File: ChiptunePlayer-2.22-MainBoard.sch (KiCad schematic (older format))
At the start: 7 parts, among them J1 USB_OTG

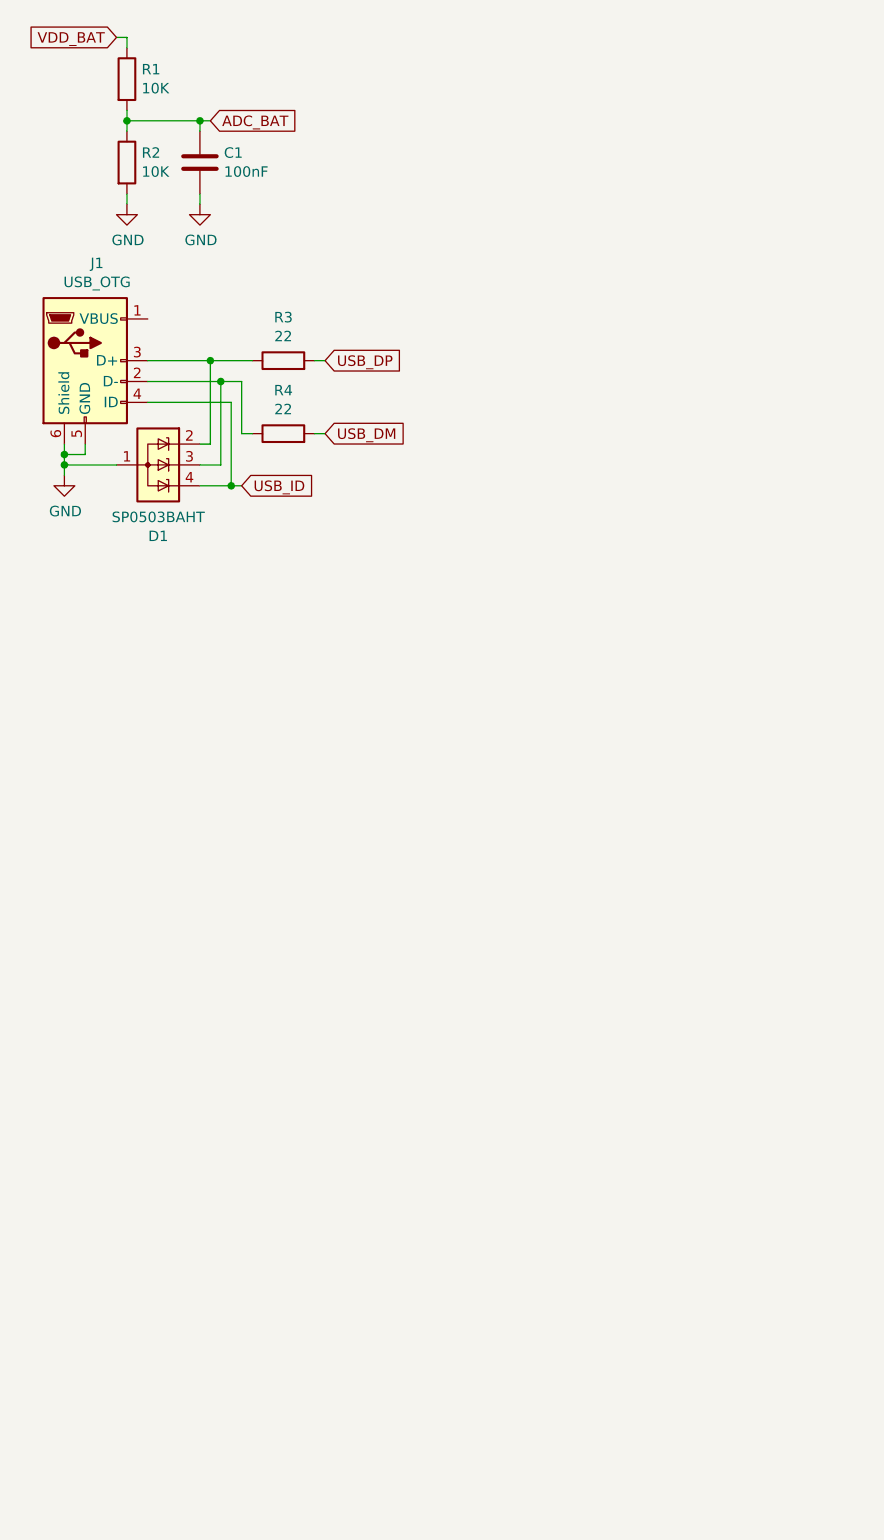
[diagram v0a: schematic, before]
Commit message: Добавлена часть зарядки, клавиши +-, поправлен USB, все разделено на вложенные листи.
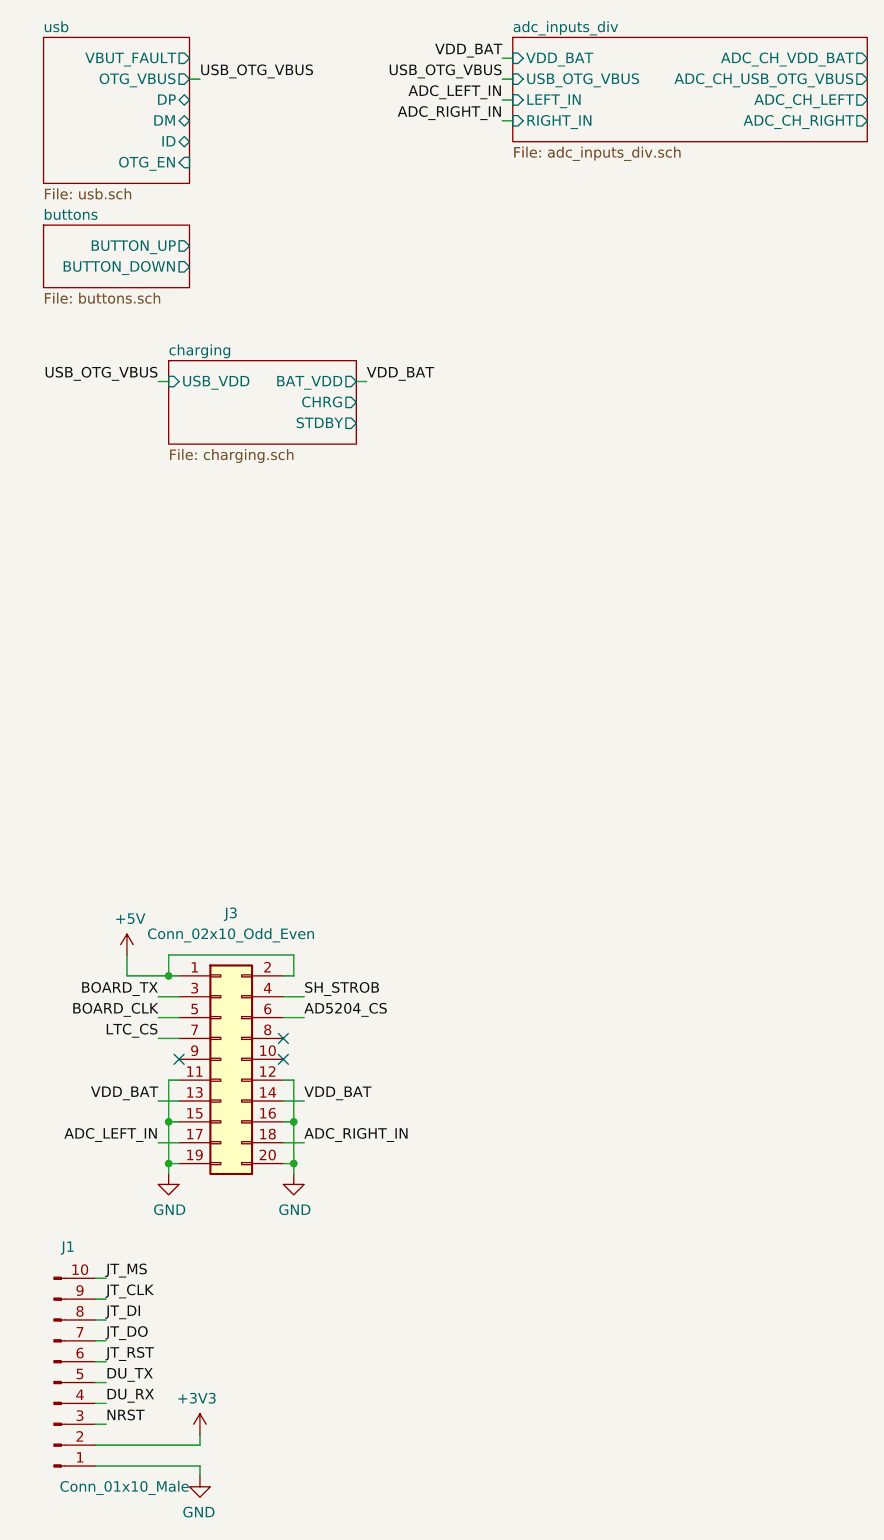
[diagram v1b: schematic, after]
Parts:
- removed C1: 100nF, Capacitor_SMD:C_0603_1608Metric_Pad1.05x0.95mm_HandSolder, symbol Device:C
- removed D1: SP0503BAHT, Package_TO_SOT_SMD:SOT-143, symbol Power_Protection:SP0503BAHT
- removed J1: USB_OTG, Connector_USB:USB_Mini-B_Wuerth_65100516121_Horizontal, symbol Connector:USB_OTG
- removed R1, R2: 10K, Resistor_SMD:R_0603_1608Metric_Pad1.05x0.95mm_HandSolder, symbol Device:R
- removed R3, R4: 22, Resistor_SMD:R_0603_1608Metric_Pad1.05x0.95mm_HandSolder, symbol Device:R
- added J1: Conn_01x10_Male, Connector_PinHeader_2.54mm:PinHeader_1x10_P2.54mm_Horizontal, symbol Connector:Conn_01x10_Male
- added J3: Conn_02x10_Odd_Even, Connector_PinHeader_2.54mm:PinHeader_2x10_P2.54mm_Vertical_SMD, symbol Connector_Generic:Conn_02x10_Odd_Even
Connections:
- net GND: now also J1.1 (Pin_1), J3.11 (Pin_11), J3.12 (Pin_12), J3.15 (Pin_15), J3.16 (Pin_16), J3.19 (Pin_19), J3.20 (Pin_20)
- net VDD_BAT: now also J3.13 (Pin_13), J3.14 (Pin_14)
- new net +3V3: J1.2 (Pin_2)
- new net +5V: J3.1 (Pin_1), J3.2 (Pin_2)
- new net AD5204_CS: J3.6 (Pin_6)
- new net ADC_LEFT_IN: J3.17 (Pin_17)
- new net ADC_RIGHT_IN: J3.18 (Pin_18)
- new net BOARD_CLK: J3.5 (Pin_5)
- new net BOARD_TX: J3.3 (Pin_3)
- new net DU_RX: J1.4 (Pin_4)
- new net DU_TX: J1.5 (Pin_5)
- new net JT_CLK: J1.9 (Pin_9)
- new net JT_DI: J1.8 (Pin_8)
- new net JT_DO: J1.7 (Pin_7)
- new net JT_MS: J1.10 (Pin_10)
- new net JT_RST: J1.6 (Pin_6)
- new net LTC_CS: J3.7 (Pin_7)
- new net NRST: J1.3 (Pin_3)
- new net SH_STROB: J3.4 (Pin_4)
- no-connect marks 0 -> 3

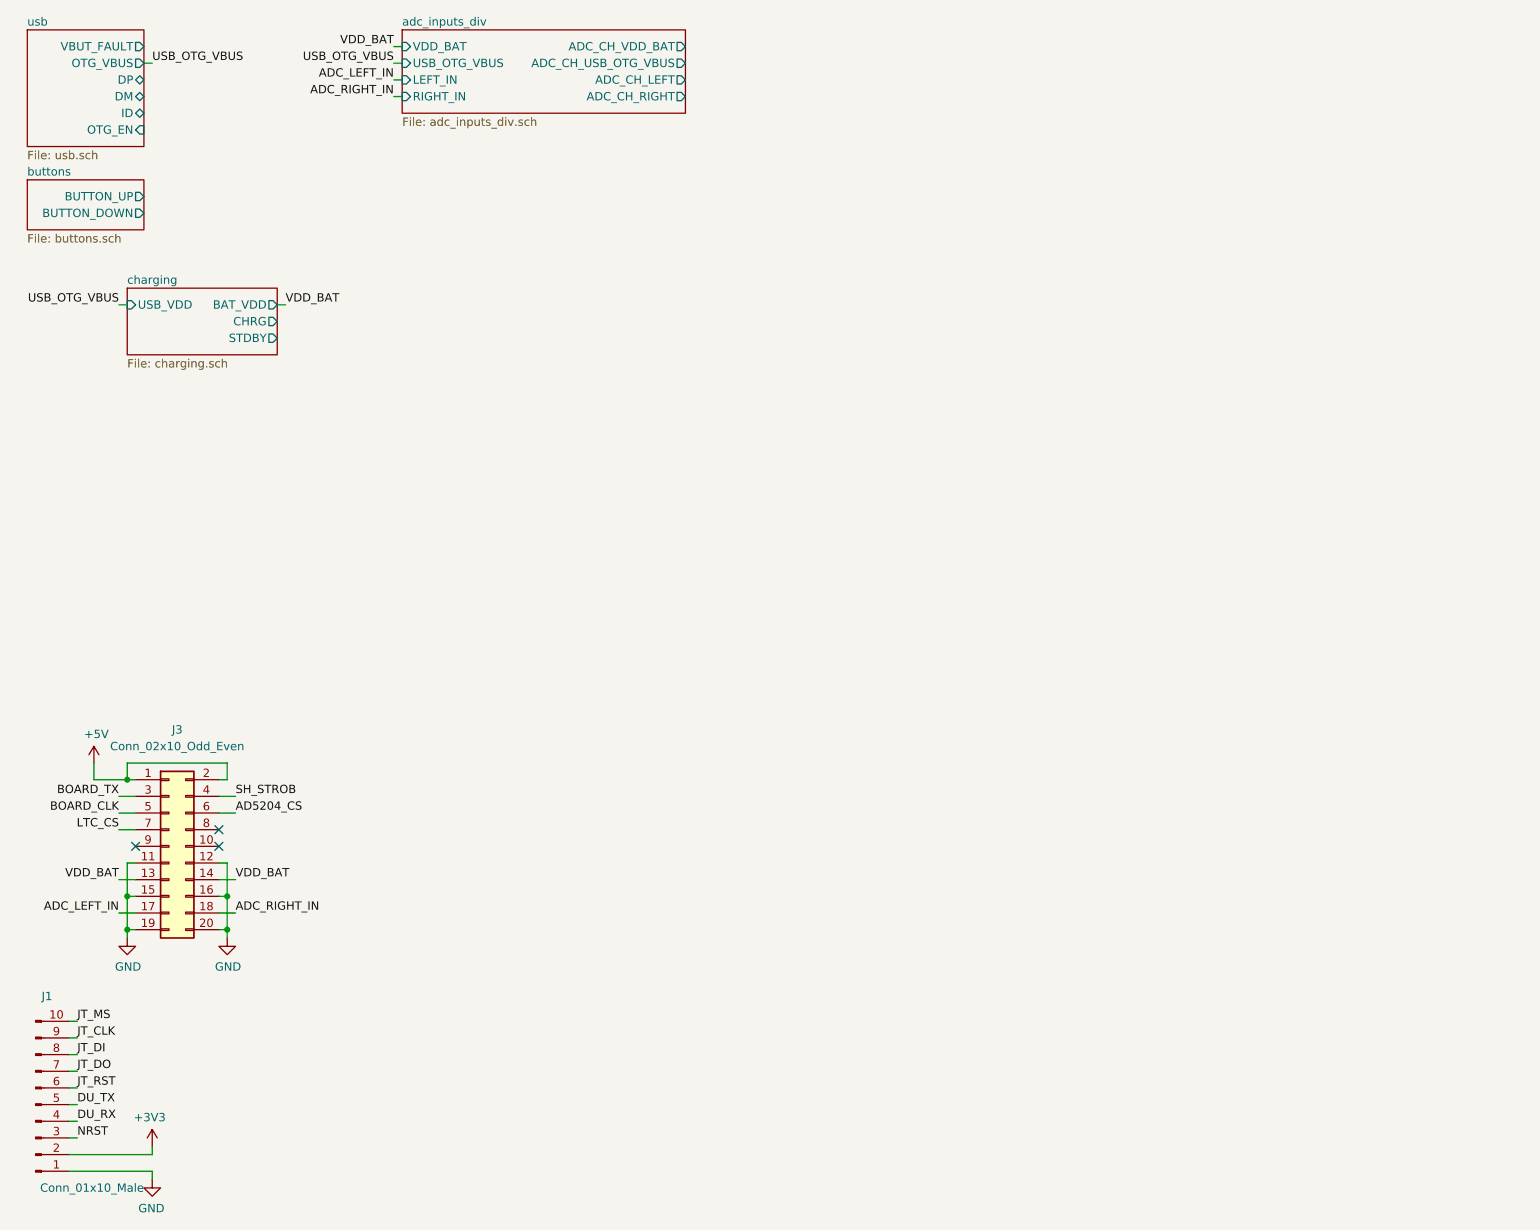
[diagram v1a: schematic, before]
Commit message: Запитал МК, добавил цепи питания, тактирования, модуль клавиатуры.
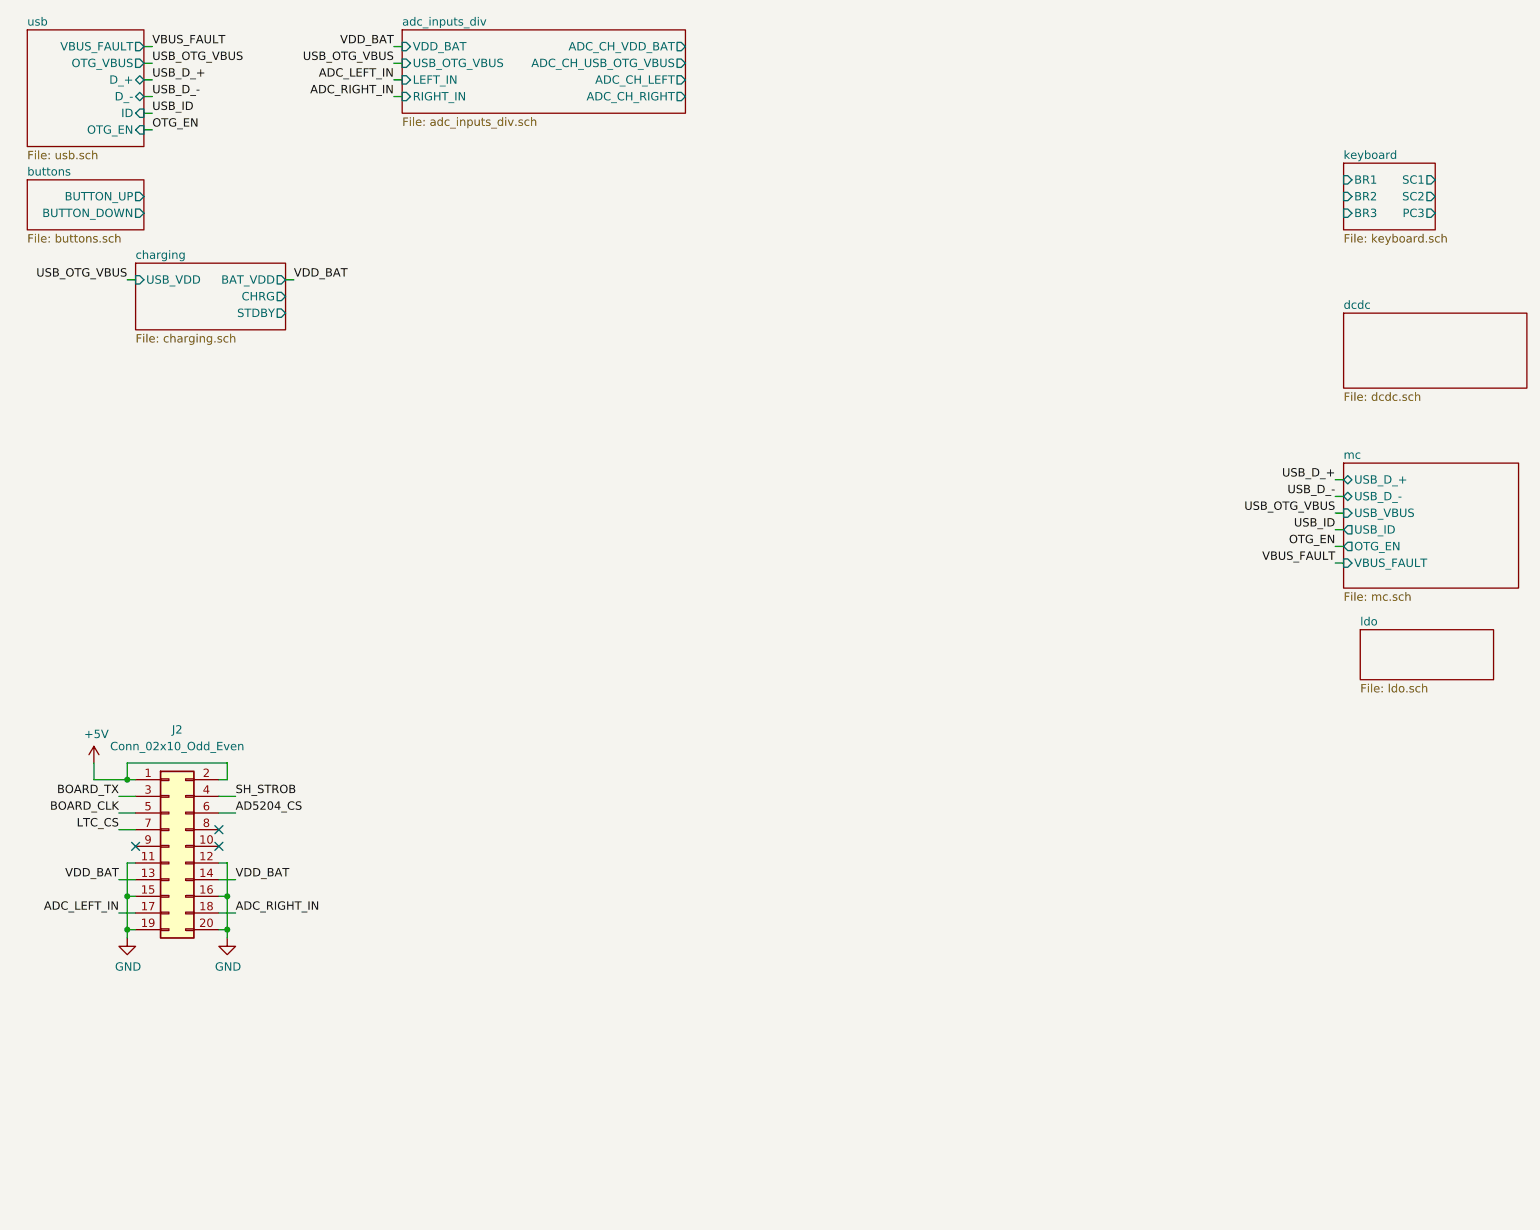
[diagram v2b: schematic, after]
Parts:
- removed J1: Conn_01x10_Male, Connector_PinHeader_2.54mm:PinHeader_1x10_P2.54mm_Horizontal, symbol Connector:Conn_01x10_Male
- renumbered J3 to J2
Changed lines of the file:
@@
 $Descr A4 11693 8268
 encoding utf-8
-Sheet 1 5
+Sheet 1 9
 Title ""
 Date "2020-04-18"
@@
 $EndDescr
 $Comp
-L Connector:Conn_01x10_Male J1
-U 1 1 5EA8D1A2
-P 600 7050
-F 0 "J1" H 700 6400 50  0000 R CNN
-F 1 "Conn_01x10_Male" H 1250 7550 50  0000 R CNN
-F 2 "Connector_PinHeader_2.54mm:PinHeader_1x10_P2.54mm_Horizontal" H 600 7050 50  0001 C CNN
-F 3 "~" H 600 7050 50  0001 C CNN
-	1    600  7050
-	1    0    0    1
-$EndComp
-$Comp
-L power:GND #PWR02
-U 1 1 5EA97B30
-P 1300 7500
-F 0 "#PWR02" H 1300 7250 50  0001 C CNN
-F 1 "GND" H 1305 7327 50  0000 C CNN
-F 2 "" H 1300 7500 50  0001 C CNN
-F 3 "" H 1300 7500 50  0001 C CNN
-	1    1300 7500
-	-1   0    0    -1
-$EndComp
-$Comp
-L power:+3V3 #PWR01
-U 1 1 5EA9CF13
-P 1300 7300
-F 0 "#PWR01" H 1300 7150 50  0001 C CNN
-F 1 "+3V3" H 1315 7473 50  0000 C CNN
-F 2 "" H 1300 7300 50  0001 C CNN
-F 3 "" H 1300 7300 50  0001 C CNN
-	1    1300 7300
-	-1   0    0    -1
-$EndComp
-Wire Wire Line
-	800  7450 1300 7450
-Wire Wire Line
-	1300 7450 1300 7500
-Wire Wire Line
-	1300 7350 1300 7300
-Wire Wire Line
-	1300 7350 800  7350
-Wire Wire Line
-	850  6550 800  6550
-Wire Wire Line
-	850  6650 800  6650
-Wire Wire Line
-	850  6750 800  6750
-Wire Wire Line
-	850  6850 800  6850
-Wire Wire Line
-	850  6950 800  6950
-Wire Wire Line
-	800  7050 850  7050
-Wire Wire Line
-	850  7150 800  7150
-Wire Wire Line
-	850  7250 800  7250
-$Comp
-L power:+5V #PWR03
+L power:+5V #PWR01
 U 1 1 5EABF65B
 P 950 5000
-F 0 "#PWR03" H 950 4850 50  0001 C CNN
+F 0 "#PWR01" H 950 4850 50  0001 C CNN
 F 1 "+5V" H 965 5173 50  0000 C CNN
 F 2 "" H 950 5000 50  0001 C CNN
@@
 $EndComp
 $Comp
-L power:GND #PWR04
+L power:GND #PWR02
 U 1 1 5EAC2A23
 P 1150 6050
-F 0 "#PWR04" H 1150 5800 50  0001 C CNN
+F 0 "#PWR02" H 1150 5800 50  0001 C CNN
 F 1 "GND" H 1155 5877 50  0000 C CNN
 F 2 "" H 1150 6050 50  0001 C CNN
@@
 $EndSheet
 $Comp
-L Connector_Generic:Conn_02x10_Odd_Even J3
+L Connector_Generic:Conn_02x10_Odd_Even J2
 U 1 1 5EA4935C
 P 1400 5500
-F 0 "J3" H 1450 6200 50  0000 C CNN
+F 0 "J2" H 1450 6200 50  0000 C CNN
 F 1 "Conn_02x10_Odd_Even" H 1450 6100 50  0000 C CNN
 F 2 "Connector_PinHeader_2.54mm:PinHeader_2x10_P2.54mm_Vertical_SMD" H 1400 5500 50  0001 C CNN
@@
 $EndComp
 $Comp
-L power:GND #PWR07
+L power:GND #PWR05
 U 1 1 5EA53146
 P 1750 6050
-F 0 "#PWR07" H 1750 5800 50  0001 C CNN
+F 0 "#PWR05" H 1750 5800 50  0001 C CNN
 F 1 "GND" H 1755 5877 50  0000 C CNN
 F 2 "" H 1750 6050 50  0001 C CNN
@@
 Text Label 1100 5200 2    50   ~ 0
 BOARD_TX
-Text Label 850  6550 0    50   ~ 0
-JT_MS
-Text Label 850  6650 0    50   ~ 0
-JT_CLK
-Text Label 850  6750 0    50   ~ 0
-JT_DI
-Text Label 850  6850 0    50   ~ 0
-JT_DO
-Text Label 850  6950 0    50   ~ 0
-JT_RST
-Text Label 850  7050 0    50   ~ 0
-DU_TX
-Text Label 850  7150 0    50   ~ 0
-DU_RX
-Text Label 850  7250 0    50   ~ 0
-NRST
 Text Label 2750 900  2    50   ~ 0
 ADC_LEFT_IN
@@
 	2750 800  2800 800
 $Sheet
-S 1150 2150 900  400
+S 1200 2000 900  400
 U 5EA97D75
 F0 "charging" 50
 F1 "charging.sch" 50
-F2 "USB_VDD" I L 1150 2250 50
-F3 "BAT_VDD" O R 2050 2250 50
-F4 "CHRG" O R 2050 2350 50
-F5 "STDBY" O R 2050 2450 50
-$EndSheet
+F2 "USB_VDD" I L 1200 2100 50
+F3 "BAT_VDD" O R 2100 2100 50
+F4 "CHRG" O R 2100 2200 50
+F5 "STDBY" O R 2100 2300 50
+$EndSheet
+Text Label 2150 2100 0    50   ~ 0
+VDD_BAT
+Wire Wire Line
+	2100 2100 2150 2100
+Text Label 1150 2100 2    50   ~ 0
+USB_OTG_VBUS
+Wire Wire Line
+	1150 2100 1200 2100
+NoConn ~ 1700 5400
+NoConn ~ 1700 5500
+NoConn ~ 1200 5500
+$Sheet
+S 8450 2300 1100 450
+U 5E9B0FB9
+F0 "dcdc" 50
+F1 "dcdc.sch" 50
+$EndSheet
+$Sheet
+S 8450 3200 1050 750
+U 5E9B10E6
+F0 "mc" 50
+F1 "mc.sch" 50
+F2 "USB_D_+" B L 8450 3300 50
+F3 "USB_D_-" B L 8450 3400 50
+F4 "USB_VBUS" I L 8450 3500 50
+F5 "USB_ID" O L 8450 3600 50
+F6 "OTG_EN" O L 8450 3700 50
+F7 "VBUS_FAULT" I L 8450 3800 50
+$EndSheet
+$Sheet
+S 8550 4200 800  300
+U 5E9B1331
+F0 "ldo" 50
+F1 "ldo.sch" 50
+$EndSheet
+$Sheet
+S 8450 1400 550  400
+U 5E9B1427
+F0 "keyboard" 50
+F1 "keyboard.sch" 50
+F2 "BR1" I L 8450 1500 50
+F3 "BR2" I L 8450 1600 50
+F4 "BR3" I L 8450 1700 50
+F5 "SC1" O R 9000 1500 50
+F6 "SC2" O R 9000 1600 50
+F7 "PC3" O R 9000 1700 50
+$EndSheet
+Wire Wire Line
+	1250 900  1300 900
+Wire Wire Line
+	1250 1000 1300 1000
+Text Label 1300 900  0    50   ~ 0
+USB_D_+
+Text Label 1300 1000 0    50   ~ 0
+USB_D_-
 $Sheet
 S 550  600  700  700
@@
 F0 "usb" 50
 F1 "usb.sch" 50
-F2 "VBUT_FAULT" O R 1250 700 50
-F3 "OTG_VBUS" O R 1250 800 50
-F4 "DP" B R 1250 900 50
-F5 "DM" B R 1250 1000 50
-F6 "ID" B R 1250 1100 50
-F7 "OTG_EN" I R 1250 1200 50
-$EndSheet
-Text Label 2100 2250 0    50   ~ 0
-VDD_BAT
-Wire Wire Line
-	2050 2250 2100 2250
-Text Label 1100 2250 2    50   ~ 0
-USB_OTG_VBUS
-Wire Wire Line
-	1100 2250 1150 2250
-NoConn ~ 1700 5400
-NoConn ~ 1700 5500
-NoConn ~ 1200 5500
+F2 "OTG_VBUS" O R 1250 800 50
+F3 "OTG_EN" I R 1250 1200 50
+F4 "D_+" B R 1250 900 50
+F5 "D_-" B R 1250 1000 50
+F6 "VBUS_FAULT" O R 1250 700 50
+F7 "ID" I R 1250 1100 50
+$EndSheet
+Text Label 8400 3500 2    50   ~ 0
+USB_OTG_VBUS
+Text Label 8400 3300 2    50   ~ 0
+USB_D_+
+Text Label 8400 3400 2    50   ~ 0
+USB_D_-
+Text Label 1300 1100 0    50   ~ 0
+USB_ID
+Text Label 8400 3600 2    50   ~ 0
+USB_ID
+Text Label 8400 3700 2    50   ~ 0
+OTG_EN
+Text Label 8400 3800 2    50   ~ 0
+VBUS_FAULT
+Text Label 1300 700  0    50   ~ 0
+VBUS_FAULT
+Text Label 1300 1200 0    50   ~ 0
+OTG_EN
+Wire Wire Line
+	1250 700  1300 700
+Wire Wire Line
+	1250 1100 1300 1100
+Wire Wire Line
+	1250 1200 1300 1200
+Wire Wire Line
+	8400 3300 8450 3300
+Wire Wire Line
+	8400 3400 8450 3400
+Wire Wire Line
+	8400 3500 8450 3500
+Wire Wire Line
+	8400 3600 8450 3600
+Wire Wire Line
+	8400 3700 8450 3700
+Wire Wire Line
+	8400 3800 8450 3800
 $EndSCHEMATC
